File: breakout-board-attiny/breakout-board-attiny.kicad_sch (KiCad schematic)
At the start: 6 parts, among them J1 Conn_01x07_Male, J2 Conn_01x07_Male, U1 ATtiny424-X

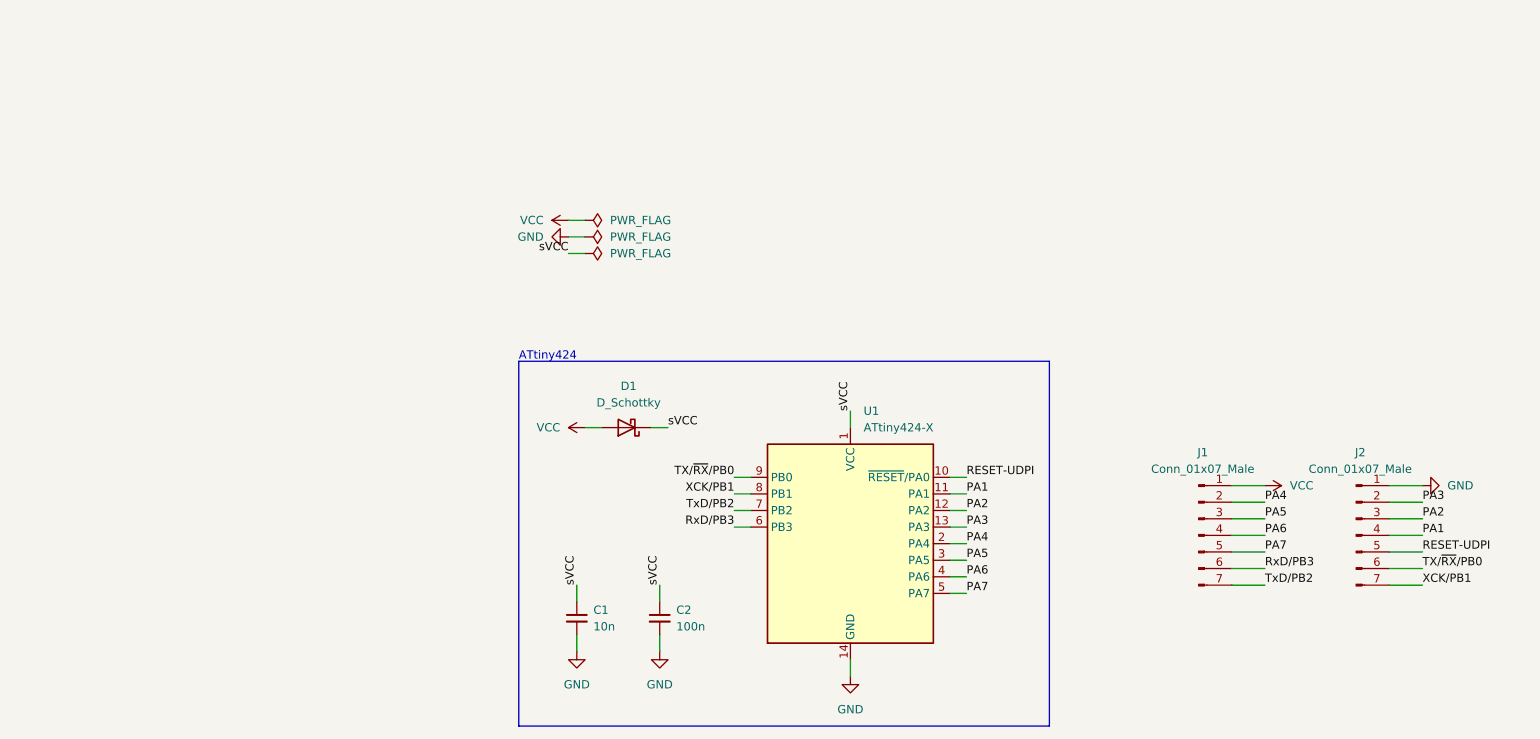
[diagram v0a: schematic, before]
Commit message: der Schaltplan des attiny breakout boards wurde verschönert
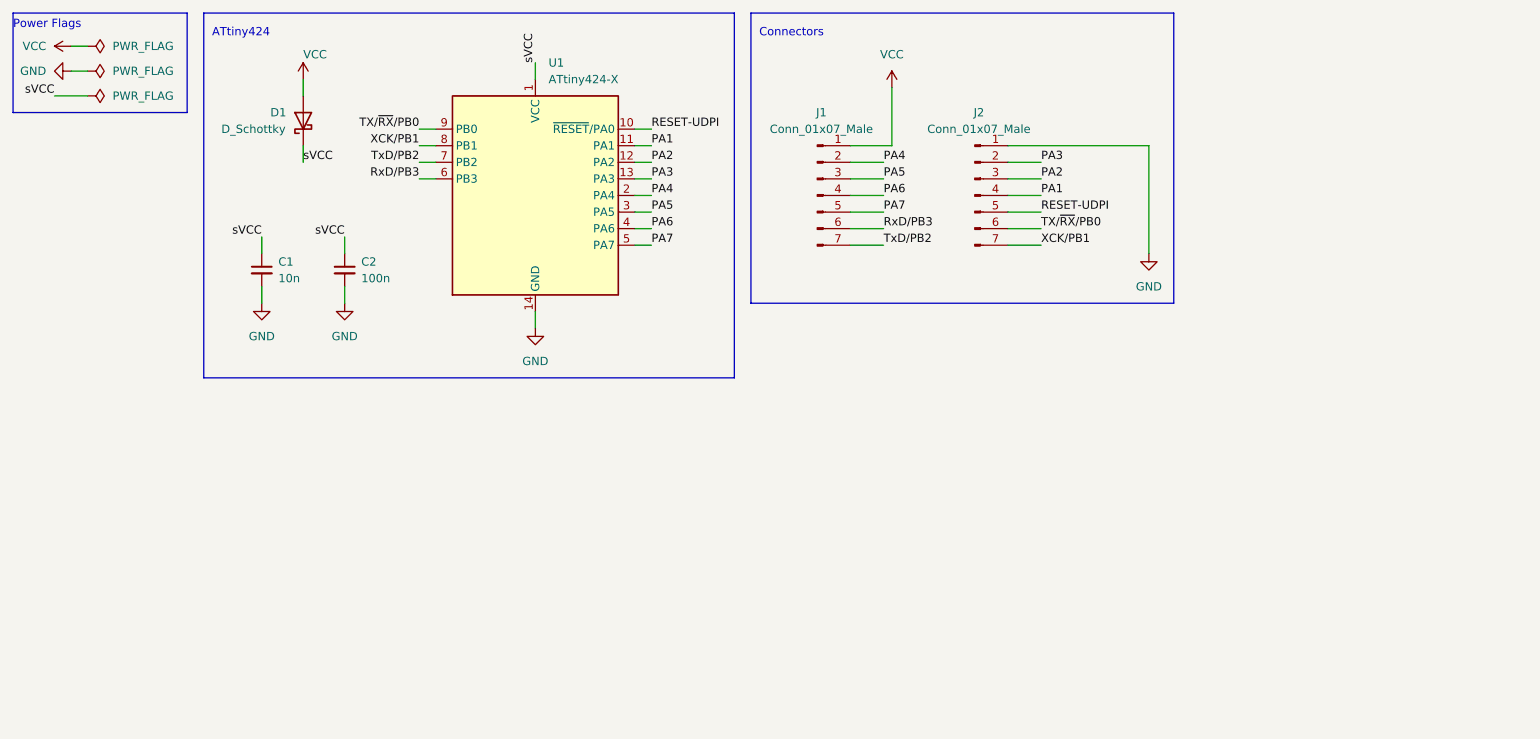
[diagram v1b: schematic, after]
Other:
- note added: "Connectors"
- note added: "Power Flags"
- moved on the sheet: C1, C2, D1, J1, J2, U1

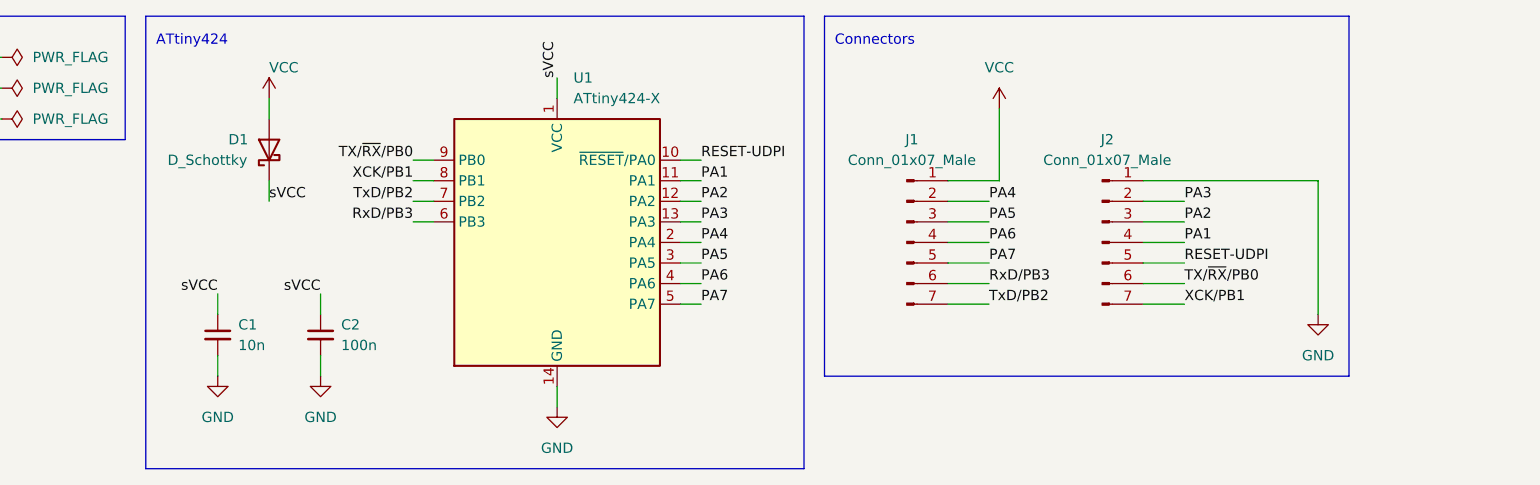
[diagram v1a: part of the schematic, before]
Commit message: Das atTiny breajout board ist fertig!
Laci hat einige Dinge an den breakout boards geändert
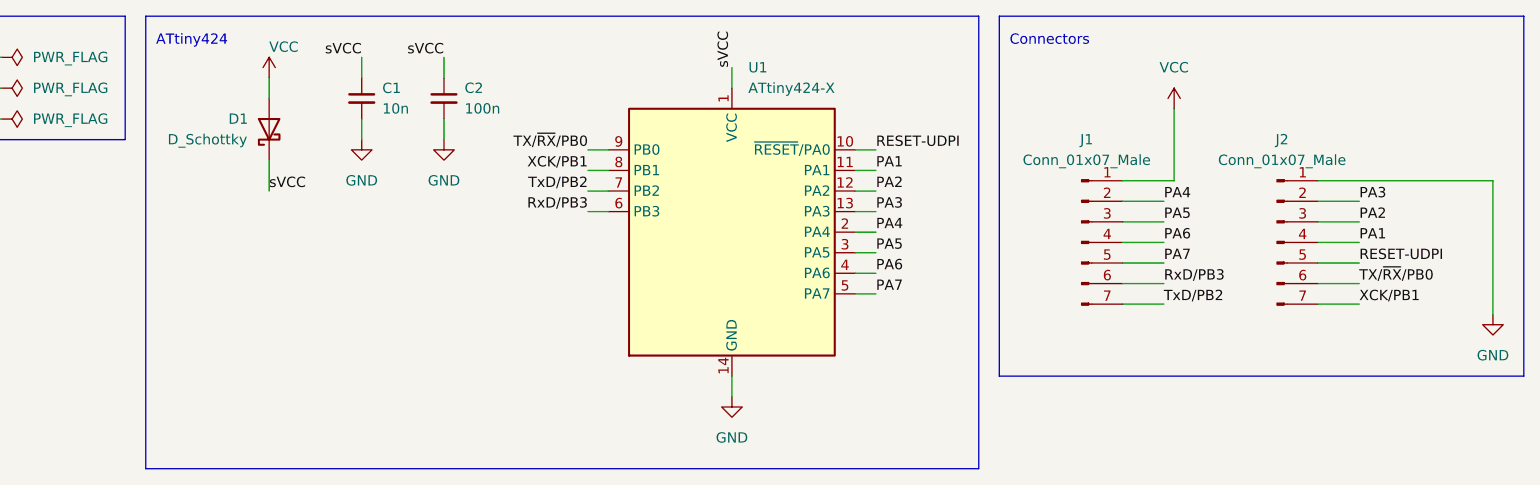
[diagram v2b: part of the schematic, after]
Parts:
- J1, J2: footprint Connector_PinHeader_2.54mm:PinHeader_1x07_P2.54mm_Vertical -> Connector_PinSocket_2.54mm:PinSocket_1x07_P2.54mm_Vertical
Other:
- moved on the sheet: C1, C2, D1, J1, J2, U1

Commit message: ATtiny breakout board done
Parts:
- added D2: LED_Small, Diode_SMD:D_1206_3216Metric, symbol Device:LED_Small
- added R1: 330, Resistor_SMD:R_1206_3216Metric, symbol Device:R_Small
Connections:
- net GND: now also D2.1 (K)
- net TxD/PB2: now also R1.1
- net PA1 renamed TXD/PA1
- net PA2 renamed RXD/PA2
- net PA3 renamed XCK/PA3
- net PA4 renamed XDIR/PA4
- net TX/~{RX}/PB0 renamed SCL/XDIR/PB0
- net XCK/PB1 renamed SDA/XCK/PB1
- new net: D2.2 (A), R1.2
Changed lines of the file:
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@@
+    (stroke (width 0) (type default))
+  )
+  (wire (pts (xy 58.42 59.69) (xy 58.42 60.96))
     (stroke (width 0) (type default))
   )
@@
     (stroke (width 0) (type default))
   )
+  (wire (pts (xy 58.42 53.34) (xy 58.42 54.61))
+    (stroke (width 0) (type default))
+  )
   (polyline (pts (xy 148.59 13.97) (xy 148.59 58.42))
     (stroke (width 0) (type default))
@@
     (stroke (width 0) (type default))
   )
+  (wire (pts (xy 58.42 45.72) (xy 58.42 48.26))
+    (stroke (width 0) (type default))
+  )
   (wire (pts (xy 80.01 26.67) (xy 80.01 29.21))
     (stroke (width 0) (type default))
@@
     (effects (font (size 1.27 1.27)) (justify left bottom))
   )
+  (label "XCK{slash}PA3" (at 193.04 36.83 0) (fields_autoplaced)
+    (effects (font (size 1.27 1.27)) (justify left bottom))
+  )
+  (label "SDA{slash}XCK{slash}PB1" (at 193.04 49.53 0) (fields_autoplaced)
+    (effects (font (size 1.27 1.27)) (justify left bottom))
+  )
+  (label "RXD{slash}PA2" (at 193.04 39.37 0) (fields_autoplaced)
+    (effects (font (size 1.27 1.27)) (justify left bottom))
+  )
   (label "sVCC" (at 58.42 35.56 0) (fields_autoplaced)
     (effects (font (size 1.27 1.27)) (justify left bottom))
@@
     (effects (font (size 1.27 1.27)) (justify right bottom))
   )
-  (label "XCK{slash}PB1" (at 193.04 49.53 0) (fields_autoplaced)
-    (effects (font (size 1.27 1.27)) (justify left bottom))
-  )
   (label "sVCC" (at 69.85 19.05 180) (fields_autoplaced)
     (effects (font (size 1.27 1.27)) (justify right bottom))
@@
     (effects (font (size 1.27 1.27)) (justify left bottom))
   )
-  (label "PA1" (at 133.35 33.02 0) (fields_autoplaced)
-    (effects (font (size 1.27 1.27)) (justify left bottom))
-  )
-  (label "XCK{slash}PB1" (at 97.79 33.02 180) (fields_autoplaced)
-    (effects (font (size 1.27 1.27)) (justify right bottom))
-  )
-  (label "PA3" (at 193.04 36.83 0) (fields_autoplaced)
-    (effects (font (size 1.27 1.27)) (justify left bottom))
-  )
-  (label "PA1" (at 193.04 41.91 0) (fields_autoplaced)
-    (effects (font (size 1.27 1.27)) (justify left bottom))
-  )
-  (label "PA4" (at 168.91 36.83 0) (fields_autoplaced)
+  (label "TXD{slash}PA1" (at 133.35 33.02 0) (fields_autoplaced)
+    (effects (font (size 1.27 1.27)) (justify left bottom))
+  )
+  (label "TxD{slash}PB2" (at 58.42 45.72 90) (fields_autoplaced)
+    (effects (font (size 1.27 1.27)) (justify left bottom))
+  )
+  (label "SDA{slash}XCK{slash}PB1" (at 97.79 33.02 180) (fields_autoplaced)
+    (effects (font (size 1.27 1.27)) (justify right bottom))
+  )
+  (label "XDIR{slash}PA4" (at 168.91 36.83 0) (fields_autoplaced)
     (effects (font (size 1.27 1.27)) (justify left bottom))
   )
@@
     (effects (font (size 1.27 1.27)) (justify left bottom))
   )
-  (label "PA3" (at 133.35 38.1 0) (fields_autoplaced)
+  (label "XCK{slash}PA3" (at 133.35 38.1 0) (fields_autoplaced)
+    (effects (font (size 1.27 1.27)) (justify left bottom))
+  )
+  (label "SCL{slash}XDIR{slash}PB0" (at 193.04 46.99 0) (fields_autoplaced)
     (effects (font (size 1.27 1.27)) (justify left bottom))
   )
@@
     (effects (font (size 1.27 1.27)) (justify left bottom))
   )
-  (label "TX{slash}~{RX}{slash}PB0" (at 193.04 46.99 0) (fields_autoplaced)
+  (label "TXD{slash}PA1" (at 193.04 41.91 0) (fields_autoplaced)
     (effects (font (size 1.27 1.27)) (justify left bottom))
   )
@@
     (effects (font (size 1.27 1.27)) (justify left bottom))
   )
-  (label "TX{slash}~{RX}{slash}PB0" (at 97.79 30.48 180) (fields_autoplaced)
-    (effects (font (size 1.27 1.27)) (justify right bottom))
-  )
-  (label "PA2" (at 133.35 35.56 0) (fields_autoplaced)
-    (effects (font (size 1.27 1.27)) (justify left bottom))
-  )
-  (label "PA2" (at 193.04 39.37 0) (fields_autoplaced)
-    (effects (font (size 1.27 1.27)) (justify left bottom))
-  )
-  (label "PA4" (at 133.35 40.64 0) (fields_autoplaced)
+  (label "SCL{slash}XDIR{slash}PB0" (at 97.79 30.48 180) (fields_autoplaced)
+    (effects (font (size 1.27 1.27)) (justify right bottom))
+  )
+  (label "RXD{slash}PA2" (at 133.35 35.56 0) (fields_autoplaced)
+    (effects (font (size 1.27 1.27)) (justify left bottom))
+  )
+  (label "XDIR{slash}PA4" (at 133.35 40.64 0) (fields_autoplaced)
     (effects (font (size 1.27 1.27)) (justify left bottom))
   )
@@
         (path "/ecb8b56d-7611-4c4a-9a78-47ca2865bc12"
           (reference "#PWR01") (unit 1)
+        )
+      )
+    )
+  )
+  (symbol (lib_id "power:GND") (at 58.42 60.96 0) (unit 1)
+    (in_bom yes) (on_board yes) (dnp no) (fields_autoplaced)
+    (property "Reference" "#PWR09" (at 58.42 67.31 0)
+      (effects (font (size 1.27 1.27)) hide)
+    )
+    (property "Value" "GND" (at 58.42 66.04 0)
+      (effects (font (size 1.27 1.27)))
+    )
+    (property "Footprint" "" (at 58.42 60.96 0)
+      (effects (font (size 1.27 1.27)) hide)
+    )
+    (property "Datasheet" "" (at 58.42 60.96 0)
+      (effects (font (size 1.27 1.27)) hide)
+    )
+    (pin "1")
+    (instances
+      (project "breakout-board-attiny"
+        (path "/ecb8b56d-7611-4c4a-9a78-47ca2865bc12"
+          (reference "#PWR09") (unit 1)
         )
       )
@@
     )
   )
+  (symbol (lib_id "Device:LED_Small") (at 58.42 57.15 90) (unit 1)
+    (in_bom yes) (on_board yes) (dnp no) (fields_autoplaced)
+    (property "Reference" "D2" (at 60.96 56.4515 90)
+      (effects (font (size 1.27 1.27)) (justify right))
+    )
+    (property "Value" "LED_Small" (at 60.96 58.9915 90)
+      (effects (font (size 1.27 1.27)) (justify right))
+    )
+    (property "Footprint" "Diode_SMD:D_1206_3216Metric" (at 58.42 57.15 90)
+      (effects (font (size 1.27 1.27)) hide)
+    )
+    (property "Datasheet" "~" (at 58.42 57.15 90)
+      (effects (font (size 1.27 1.27)) hide)
+    )
+    (pin "1")
+    (pin "2")
+    (instances
+      (project "breakout-board-attiny"
+        (path "/ecb8b56d-7611-4c4a-9a78-47ca2865bc12"
+          (reference "D2") (unit 1)
+        )
+      )
+    )
+  )
   (symbol (lib_id "power:GND") (at 209.55 50.8 0) (unit 1)
     (in_bom yes) (on_board yes) (dnp no) (fields_autoplaced)
@@
         )
       )
+    )
+  )
+  (symbol (lib_id "Device:R_Small") (at 58.42 50.8 0) (unit 1)
+    (in_bom yes) (on_board yes) (dnp no) (fields_autoplaced)
+    (property "Reference" "R1" (at 60.96 50.165 0)
+      (effects (font (size 1.27 1.27)) (justify left))
+    )
+    (property "Value" "330" (at 60.96 52.705 0)
+      (effects (font (size 1.27 1.27)) (justify left))
+    )
+    (property "Footprint" "Resistor_SMD:R_1206_3216Metric" (at 58.42 50.8 0)
+      (effects (font (size 1.27 1.27)) hide)
+    )
+    (property "Datasheet" "~" (at 58.42 50.8 0)
+      (effects (font (size 1.27 1.27)) hide)
+    )
+    (pin "1")
+    (pin "2")
+    (instances
+      (project "breakout-board-attiny"
+        (path "/ecb8b56d-7611-4c4a-9a78-47ca2865bc12"
+          (reference "R1") (unit 1)
+        )
+      )

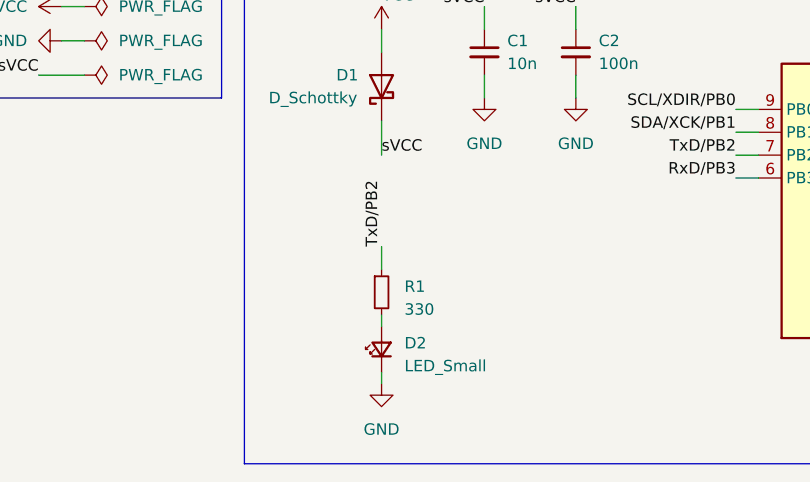
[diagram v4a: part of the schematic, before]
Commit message: ATtiny breakout board finished and ready for production
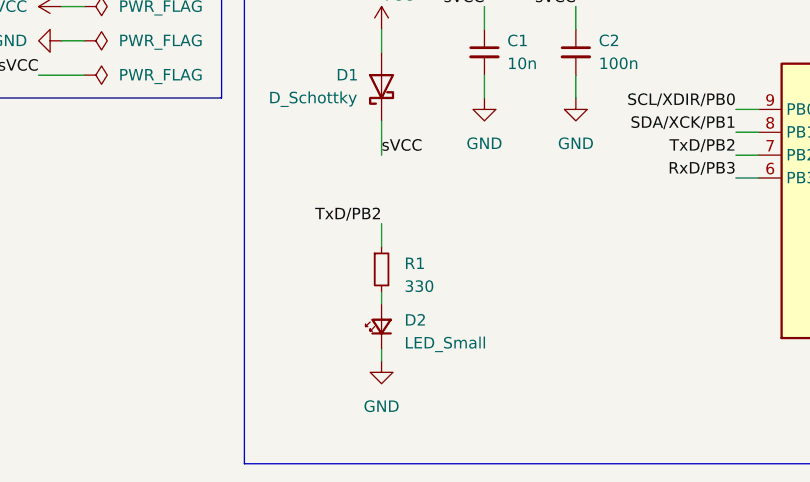
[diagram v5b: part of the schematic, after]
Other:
- moved on the sheet: D2, R1
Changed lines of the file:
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@@
     (stroke (width 0) (type default))
   )
-  (wire (pts (xy 58.42 59.69) (xy 58.42 60.96))
+  (wire (pts (xy 58.42 57.15) (xy 58.42 58.42))
     (stroke (width 0) (type default))
   )
@@
     (stroke (width 0) (type default))
   )
-  (wire (pts (xy 58.42 53.34) (xy 58.42 54.61))
+  (wire (pts (xy 58.42 50.8) (xy 58.42 52.07))
     (stroke (width 0) (type default))
   )
@@
     (stroke (width 0) (type default))
   )
-  (wire (pts (xy 58.42 45.72) (xy 58.42 48.26))
+  (wire (pts (xy 58.42 43.18) (xy 58.42 45.72))
     (stroke (width 0) (type default))
   )
@@
     (effects (font (size 1.27 1.27)) (justify left bottom))
   )
-  (label "TxD{slash}PB2" (at 58.42 45.72 90) (fields_autoplaced)
-    (effects (font (size 1.27 1.27)) (justify left bottom))
+  (label "TxD{slash}PB2" (at 58.42 43.18 180) (fields_autoplaced)
+    (effects (font (size 1.27 1.27)) (justify right bottom))
   )
   (label "SDA{slash}XCK{slash}PB1" (at 97.79 33.02 180) (fields_autoplaced)
@@
     )
   )
-  (symbol (lib_id "power:GND") (at 58.42 60.96 0) (unit 1)
-    (in_bom yes) (on_board yes) (dnp no) (fields_autoplaced)
-    (property "Reference" "#PWR09" (at 58.42 67.31 0)
-      (effects (font (size 1.27 1.27)) hide)
-    )
-    (property "Value" "GND" (at 58.42 66.04 0)
-      (effects (font (size 1.27 1.27)))
-    )
-    (property "Footprint" "" (at 58.42 60.96 0)
-      (effects (font (size 1.27 1.27)) hide)
-    )
-    (property "Datasheet" "" (at 58.42 60.96 0)
+  (symbol (lib_id "power:GND") (at 58.42 58.42 0) (unit 1)
+    (in_bom yes) (on_board yes) (dnp no) (fields_autoplaced)
+    (property "Reference" "#PWR09" (at 58.42 64.77 0)
+      (effects (font (size 1.27 1.27)) hide)
+    )
+    (property "Value" "GND" (at 58.42 63.5 0)
+      (effects (font (size 1.27 1.27)))
+    )
+    (property "Footprint" "" (at 58.42 58.42 0)
+      (effects (font (size 1.27 1.27)) hide)
+    )
+    (property "Datasheet" "" (at 58.42 58.42 0)
       (effects (font (size 1.27 1.27)) hide)
     )
@@
     )
   )
-  (symbol (lib_id "Device:LED_Small") (at 58.42 57.15 90) (unit 1)
-    (in_bom yes) (on_board yes) (dnp no) (fields_autoplaced)
-    (property "Reference" "D2" (at 60.96 56.4515 90)
+  (symbol (lib_id "Device:LED_Small") (at 58.42 54.61 90) (unit 1)
+    (in_bom yes) (on_board yes) (dnp no) (fields_autoplaced)
+    (property "Reference" "D2" (at 60.96 53.9115 90)
       (effects (font (size 1.27 1.27)) (justify right))
     )
-    (property "Value" "LED_Small" (at 60.96 58.9915 90)
+    (property "Value" "LED_Small" (at 60.96 56.4515 90)
       (effects (font (size 1.27 1.27)) (justify right))
     )
-    (property "Footprint" "Diode_SMD:D_1206_3216Metric" (at 58.42 57.15 90)
-      (effects (font (size 1.27 1.27)) hide)
-    )
-    (property "Datasheet" "~" (at 58.42 57.15 90)
+    (property "Footprint" "Diode_SMD:D_1206_3216Metric" (at 58.42 54.61 90)
+      (effects (font (size 1.27 1.27)) hide)
+    )
+    (property "Datasheet" "~" (at 58.42 54.61 90)
       (effects (font (size 1.27 1.27)) hide)
     )
@@
     )
   )
-  (symbol (lib_id "Device:R_Small") (at 58.42 50.8 0) (unit 1)
-    (in_bom yes) (on_board yes) (dnp no) (fields_autoplaced)
-    (property "Reference" "R1" (at 60.96 50.165 0)
-      (effects (font (size 1.27 1.27)) (justify left))
-    )
-    (property "Value" "330" (at 60.96 52.705 0)
-      (effects (font (size 1.27 1.27)) (justify left))
-    )
-    (property "Footprint" "Resistor_SMD:R_1206_3216Metric" (at 58.42 50.8 0)
-      (effects (font (size 1.27 1.27)) hide)
-    )
-    (property "Datasheet" "~" (at 58.42 50.8 0)
-      (effects (font (size 1.27 1.27)) hide)
-    )
+  (symbol (lib_id "Device:R_Small") (at 58.42 48.26 0) (unit 1)
+    (in_bom yes) (on_board yes) (dnp no) (fields_autoplaced)
+    (property "Reference" "R1" (at 60.96 47.625 0)
+      (effects (font (size 1.27 1.27)) (justify left))
+    )
+    (property "Value" "330" (at 60.96 50.165 0)
+      (effects (font (size 1.27 1.27)) (justify left))
+    )
+    (property "Footprint" "Resistor_SMD:R_1206_3216Metric" (at 58.42 48.26 0)
+      (effects (font (size 1.27 1.27)) hide)
+    )
+    (property "Datasheet" "~" (at 58.42 48.26 0)
+      (effects (font (size 1.27 1.27)) hide)
+    )
